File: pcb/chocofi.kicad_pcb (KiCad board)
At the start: 2 copper layers, 111.3 x 90 mm, 58 parts, among them J1 MJ-4PP-9, J2 OLED, SW10 SW_PUSH, SW11 SW_PUSH, SW12 SW_PUSH, SW14 SW_PUSH, SW15 SW_PUSH, SW16 SW_PUSH, SW17 SW_PUSH, SW18 SW_PUSH, SW19 SW_PUSH, SW2 SW_PUSH, SW20 SW_PUSH, SW21 SW_PUSH, SW3 SW_PUSH, SW4 SW_PUSH, SW5 SW_PUSH, SW6 SW_PUSH, SW8 SW_PUSH, SW9 SW_PUSH, U1 ProMicro

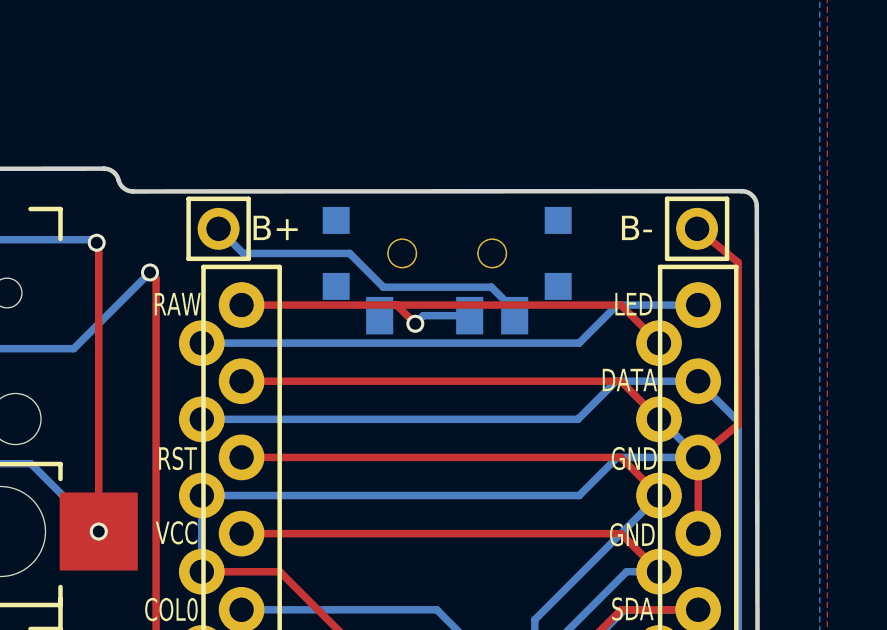
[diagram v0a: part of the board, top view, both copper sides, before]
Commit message: feat: add reversable switch
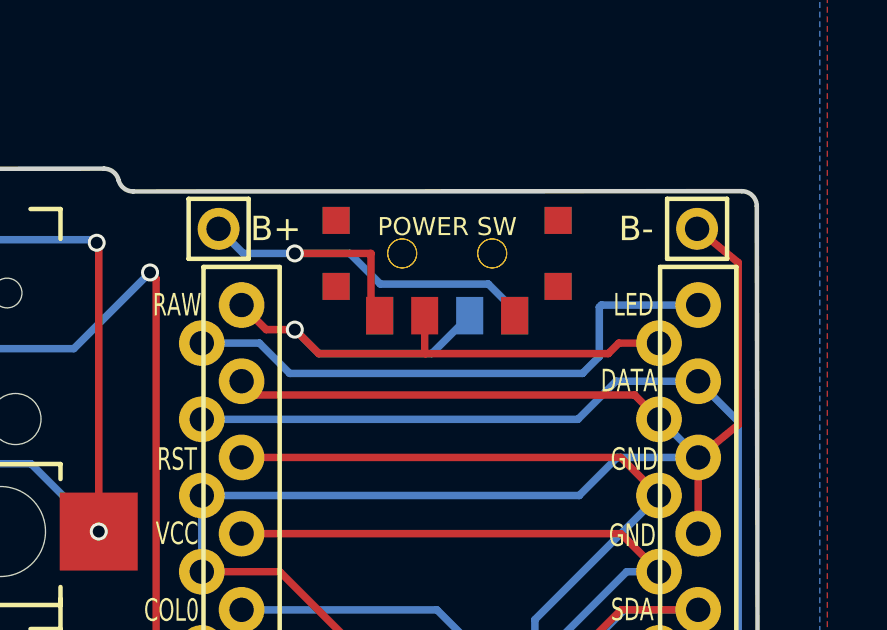
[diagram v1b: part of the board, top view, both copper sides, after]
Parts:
- added POWER SW: SW_SPDT, Kailh:SPDT_C128955, F.Cu at (177.8, 55.9)
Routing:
- net Net-(U1-Pad24): track 17.3 -> 23.2 mm
- net bat+: track 11.2 -> 15.9 mm, vias 0 -> 1
- net LED: track 17.1 -> 18.9 mm
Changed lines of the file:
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@@
     (pad "h5" thru_hole circle locked (at 0 0) (size 4 4) (drill 3.8) (layers *.Cu *.Mask))
+  )
+  (footprint "Kailh:SPDT_C128955" (layer "F.Cu")
+    (at 177.8 55.88)
+    (attr through_hole)
+    (fp_text reference "POWER SW" (at 0 -0.889) (layer "F.SilkS")
+      (effects (font (size 0.6 0.6) (thickness 0.12)))
+    )
+    (fp_text value "SW_SPDT" (at -0.05 -4.7) (layer "F.Fab")
+      (effects (font (size 1 1) (thickness 0.15)))
+    )
+    (fp_line (start 0 -1.35) (end 3.3 -1.35) (layer "F.Fab") (width 0.15))
+    (fp_line (start -1.95 -1.35) (end -1.95 -3.85) (layer "F.Fab") (width 0.15))
+    (fp_line (start 3.3 1.5) (end 3.3 -1.35) (layer "F.Fab") (width 0.15))
+    (fp_line (start -3.3 -1.35) (end -3.3 1.5) (layer "F.Fab") (width 0.15))
+    (fp_line (start -3.3 1.5) (end 3.3 1.5) (layer "F.Fab") (width 0.15))
+    (fp_line (start 0 -1.35) (end -3.3 -1.35) (layer "F.Fab") (width 0.15))
+    (fp_line (start -1.95 -3.85) (end 0 -3.85) (layer "F.Fab") (width 0.15))
+    (fp_line (start 1.9 -3.85) (end 1.95 -1.35) (layer "F.Fab") (width 0.15))
+    (fp_line (start 1.95 -1.35) (end -1.95 -1.35) (layer "F.Fab") (width 0.15))
+    (fp_line (start 0 -3.85) (end 1.9 -3.85) (layer "F.Fab") (width 0.15))
+    (pad "" np_thru_hole circle locked (at 1.5 0) (size 1 1) (drill 0.9) (layers F&B.Cu *.Mask))
+    (pad "" np_thru_hole circle locked (at -1.5 0) (size 1 1) (drill 0.9) (layers F&B.Cu *.Mask))
+    (pad "0" smd rect locked (at -3.7 -1.1) (size 0.9 0.9) (layers "F.Cu" "F.Paste" "F.Mask"))
+    (pad "0" smd rect locked (at -3.7 1.1) (size 0.9 0.9) (layers "F.Cu" "F.Paste" "F.Mask"))
+    (pad "0" smd rect locked (at 3.7 -1.1) (size 0.9 0.9) (layers "F.Cu" "F.Paste" "F.Mask"))
+    (pad "0" smd rect locked (at 3.7 1.1) (size 0.9 0.9) (layers "F.Cu" "F.Paste" "F.Mask"))
+    (pad "1" smd rect locked (at 2.25 2.075) (size 0.9 1.25) (layers "F.Cu" "F.Paste" "F.Mask"))
+    (pad "2" smd rect locked (at -0.75 2.075) (size 0.9 1.25) (layers "F.Cu" "F.Paste" "F.Mask")
+      (net 41 "Net-(U1-Pad24)"))
+    (pad "3" smd rect locked (at -2.25 2.075) (size 0.9 1.25) (layers "F.Cu" "F.Paste" "F.Mask")
+      (net 42 "bat+"))
   )
   (footprint "kbd:1pin_conn" (layer "F.Cu")
@@
   (segment (start 172.222 66.4904) (end 169.62 66.4904) (width 0.25) (layer "F.Cu") (net 23))
   (segment (start 187.5 61.5934) (end 186.1664 62.6804) (width 0.25) (layer "F.Cu") (net 23))
+  (segment (start 171.406 60.6) (end 184.0496 60.6) (width 0.25) (layer "F.Cu") (net 23))
   (segment (start 186.003 93.853) (end 184.5076 95.3484) (width 0.25) (layer "F.Cu") (net 23))
   (segment (start 186.003 90.97992) (end 186.003 93.853) (width 0.25) (layer "F.Cu") (net 23))
-  (segment (start 183.59 60.1404) (end 184.86 61.4104) (width 0.25) (layer "F.Cu") (net 23))
   (segment (start 180.97002 87.43842) (end 177.8 84.2684) (width 0.25) (layer "F.Cu") (net 23))
-  (segment (start 170.9464 60.1404) (end 183.59 60.1404) (width 0.25) (layer "F.Cu") (net 23))
   (segment (start 182.2874 96.861) (end 181.66 96.861) (width 0.25) (layer "F.Cu") (net 23))
   (segment (start 177.8 84.2684) (end 174.90201 81.37041) (width 0.25) (layer "F.Cu") (net 23))
   (segment (start 184.5076 95.3484) (end 183.8 95.3484) (width 0.25) (layer "F.Cu") (net 23))
   (segment (start 174.90201 69.17041) (end 172.222 66.4904) (width 0.25) (layer "F.Cu") (net 23))
+  (segment (start 170.9464 60.1404) (end 171.406 60.6) (width 0.25) (layer "F.Cu") (net 23))
   (segment (start 181.64 87.43842) (end 182.4615 87.43842) (width 0.25) (layer "F.Cu") (net 23))
   (segment (start 186.1664 62.6804) (end 186.1664 65.2204) (width 0.25) (layer "F.Cu") (net 23))
@@
   (segment (start 174.90201 81.37041) (end 174.90201 69.17041) (width 0.25) (layer "F.Cu") (net 23))
   (segment (start 181.64 87.43842) (end 180.97002 87.43842) (width 0.25) (layer "F.Cu") (net 23))
+  (segment (start 184.0496 60.6) (end 184.86 61.4104) (width 0.25) (layer "F.Cu") (net 23))
   (segment (start 186.13 55.0604) (end 187.5 56.1838) (width 0.25) (layer "F.Cu") (net 23))
   (via (at 177.8 84.2684) (size 0.6) (drill 0.4) (layers "F.Cu" "B.Cu") (net 23))
@@
   (segment (start 158.9606 65.1256) (end 156.8594 65.1256) (width 0.25) (layer "B.Cu") (net 30))
   (segment (start 170.9464 80.4604) (end 177.455002 80.4604) (width 0.25) (layer "B.Cu") (net 30))
-  (segment (start 169.62 58.8704) (end 182.198 58.8704) (width 0.25) (layer "B.Cu") (net 31))
-  (segment (start 182.198 58.8704) (end 183.468 57.6004) (width 0.25) (layer "B.Cu") (net 31))
-  (segment (start 183.468 57.6004) (end 186.1664 57.6004) (width 0.25) (layer "B.Cu") (net 31))
+  (segment (start 169.62 58.8704) (end 171.5404 58.8704) (width 0.25) (layer "B.Cu") (net 31))
+  (segment (start 172.55 59.88) (end 182.31 59.88) (width 0.25) (layer "B.Cu") (net 31))
+  (segment (start 182.31 59.88) (end 182.87 59.32) (width 0.25) (layer "B.Cu") (net 31))
+  (segment (start 182.87 57.67) (end 182.9396 57.6004) (width 0.25) (layer "B.Cu") (net 31))
+  (segment (start 182.9396 57.6004) (end 186.1664 57.6004) (width 0.25) (layer "B.Cu") (net 31))
+  (segment (start 182.87 59.32) (end 182.87 57.67) (width 0.25) (layer "B.Cu") (net 31))
+  (segment (start 171.5404 58.8704) (end 172.55 59.88) (width 0.25) (layer "B.Cu") (net 31))
   (segment (start 184.66 96.861) (end 184.66 102.811) (width 0.25) (layer "F.Cu") (net 32))
   (segment (start 169.62 61.4104) (end 182.158 61.4104) (width 0.25) (layer "B.Cu") (net 32))
@@
   (segment (start 179.06 88.44878) (end 179.06 90.5584) (width 0.25) (layer "B.Cu") (net 39))
   (segment (start 176.16 101.061) (end 176.16 98.611) (width 0.25) (layer "F.Cu") (net 40))
-  (segment (start 183.59 57.6004) (end 184.86 58.8704) (width 0.25) (layer "F.Cu") (net 41))
-  (segment (start 176.0796 57.6004) (end 183.59 57.6004) (width 0.25) (layer "F.Cu") (net 41))
-  (segment (start 170.9464 57.6004) (end 176.0796 57.6004) (width 0.25) (layer "F.Cu") (net 41))
-  (segment (start 176.737188 58.2249) (end 176.112688 57.6004) (width 0.25) (layer "F.Cu") (net 41))
-  (segment (start 176.112688 57.6004) (end 176.0796 57.6004) (width 0.25) (layer "F.Cu") (net 41))
-  (via (at 176.737188 58.2249) (size 0.6) (drill 0.4) (layers "F.Cu" "B.Cu") (free) (net 41))
-  (segment (start 178.55 57.955) (end 177.007088 57.955) (width 0.25) (layer "B.Cu") (net 41))
-  (segment (start 177.007088 57.955) (end 176.737188 58.2249) (width 0.25) (layer "B.Cu") (net 41))
-  (segment (start 175.675 57.005) (end 174.55 55.88) (width 0.25) (layer "B.Cu") (net 42))
-  (segment (start 180.05 57.78) (end 179.275 57.005) (width 0.25) (layer "B.Cu") (net 42))
+  (segment (start 177.07 59.22) (end 183.17 59.22) (width 0.25) (layer "F.Cu") (net 41))
+  (segment (start 173.52 59.22) (end 177.07 59.22) (width 0.25) (layer "F.Cu") (net 41))
+  (segment (start 177.05 59.2) (end 177.07 59.22) (width 0.25) (layer "F.Cu") (net 41))
+  (segment (start 172.72 58.42) (end 171.766 58.42) (width 0.25) (layer "F.Cu") (net 41))
+  (segment (start 172.72 58.42) (end 173.52 59.22) (width 0.25) (layer "F.Cu") (net 41))
+  (segment (start 183.17 59.22) (end 183.5196 58.8704) (width 0.25) (layer "F.Cu") (net 41))
+  (segment (start 171.766 58.42) (end 170.9464 57.6004) (width 0.25) (layer "F.Cu") (net 41))
+  (segment (start 183.5196 58.8704) (end 184.86 58.8704) (width 0.25) (layer "F.Cu") (net 41))
+  (segment (start 177.05 57.955) (end 177.05 59.2) (width 0.25) (layer "F.Cu") (net 41))
+  (segment (start 184.4704 59.26) (end 184.86 58.8704) (width 0.25) (layer "F.Cu") (net 41))
+  (via (at 172.72 58.42) (size 0.6) (drill 0.4) (layers "F.Cu" "B.Cu") (free) (net 41))
+  (segment (start 177.285 59.22) (end 173.52 59.22) (width 0.25) (layer "B.Cu") (net 41))
+  (segment (start 173.52 59.22) (end 172.72 58.42) (width 0.25) (layer "B.Cu") (net 41))
+  (segment (start 178.55 57.955) (end 177.285 59.22) (width 0.25) (layer "B.Cu") (net 41))
+  (segment (start 172.72 55.88) (end 175.26 55.88) (width 0.25) (layer "F.Cu") (net 42))
+  (segment (start 175.26 57.665) (end 175.55 57.955) (width 0.25) (layer "F.Cu") (net 42))
+  (segment (start 175.26 55.88) (end 175.26 57.665) (width 0.25) (layer "F.Cu") (net 42))
+  (via (at 172.72 55.88) (size 0.6) (drill 0.4) (layers "F.Cu" "B.Cu") (net 42))
   (segment (start 170.9996 55.88) (end 170.18 55.0604) (width 0.25) (layer "B.Cu") (net 42))
+  (segment (start 175.57 56.9) (end 174.55 55.88) (width 0.25) (layer "B.Cu") (net 42))
+  (segment (start 174.55 55.88) (end 172.72 55.88) (width 0.25) (layer "B.Cu") (net 42))
+  (segment (start 179.17 56.9) (end 175.57 56.9) (width 0.25) (layer "B.Cu") (net 42))
   (segment (start 180.05 57.955) (end 180.05 57.78) (width 0.25) (layer "B.Cu") (net 42))
-  (segment (start 179.275 57.005) (end 175.675 57.005) (width 0.25) (layer "B.Cu") (net 42))
-  (segment (start 174.55 55.88) (end 170.9996 55.88) (width 0.25) (layer "B.Cu") (net 42))
+  (segment (start 180.05 57.78) (end 179.17 56.9) (width 0.25) (layer "B.Cu") (net 42))
+  (segment (start 172.72 55.88) (end 170.9996 55.88) (width 0.25) (layer "B.Cu") (net 42))
   (zone (net 0) (net_name "") (layer "F.Cu") (hatch edge 0.508)
     (connect_pads (clearance 0.508))
